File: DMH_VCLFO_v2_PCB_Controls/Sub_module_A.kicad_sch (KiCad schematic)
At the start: 93 parts, among them J34 Conn_02x03_Odd_Even, J35 Conn_02x03_Odd_Even, J36 Conn_02x03_Odd_Even, J37 Conn_02x03_Odd_Even, J38 Conn_02x03_Odd_Even, J39 Conn_02x03_Odd_Even, Q10 MMBFJ113, Q11 BC548, Q12 BC548, Q13 BC558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

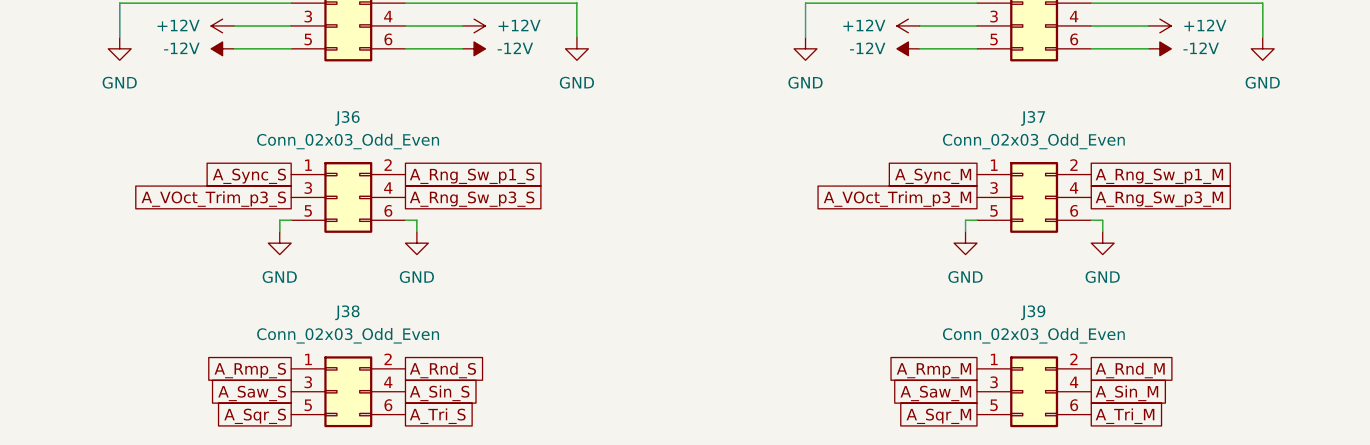
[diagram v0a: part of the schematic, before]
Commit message: Synced Controls PCB with Main
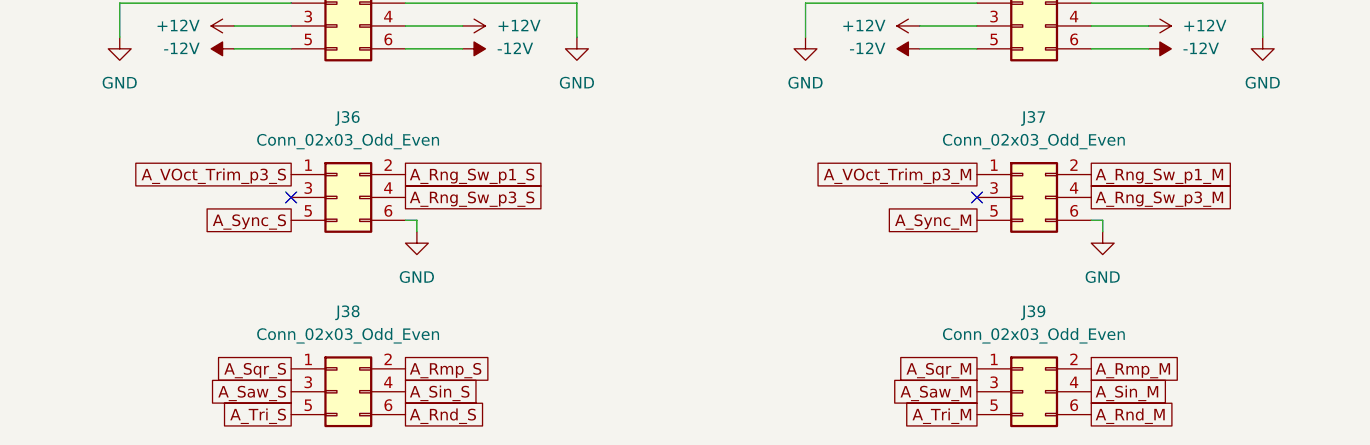
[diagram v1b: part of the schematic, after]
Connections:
- net A_Rmp_M: now also J39.2 (Pin_2); no longer J39.1 (Pin_1)
- net A_Rmp_S: now also J38.2 (Pin_2); no longer J38.1 (Pin_1)
- net A_Rnd_M: now also J39.6 (Pin_6); no longer J39.2 (Pin_2)
- net A_Rnd_S: now also J38.6 (Pin_6); no longer J38.2 (Pin_2)
- net A_Sqr_M: now also J39.1 (Pin_1); no longer J39.5 (Pin_5)
- net A_Sqr_S: now also J38.1 (Pin_1); no longer J38.5 (Pin_5)
- net A_Sync_M: now also J37.5 (Pin_5); no longer J37.1 (Pin_1)
- net A_Sync_S: now also J36.5 (Pin_5); no longer J36.1 (Pin_1)
- net A_Tri_M: now also J39.5 (Pin_5); no longer J39.6 (Pin_6)
- net A_Tri_S: now also J38.5 (Pin_5); no longer J38.6 (Pin_6)
- net A_VOct_Trim_p3_M: now also J37.1 (Pin_1); no longer J37.3 (Pin_3)
- net A_VOct_Trim_p3_S: now also J36.1 (Pin_1); no longer J36.3 (Pin_3)
- net GND: no longer J36.5 (Pin_5), J37.5 (Pin_5)
- no-connect marks 1 -> 3

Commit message: Generated Gerbers
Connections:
- net A_Rnd_S: now also U12.8, U12.9 (-); no longer U12.6 (-), U12.7
- net Comp_Ref: now also U12.2 (-); no longer U12.13 (-)
- net at D10.1 (K): now also U12.1; no longer U12.14
- net at Q9.1 (D), R71.1, R75.1: now also U12.14; no longer U12.1
- net at R71.2, R74.1: now also U12.13 (-); no longer U12.2 (-)
- net at R54.2, R61.1: now also U12.7; no longer U12.8
- net at C3.2, R73.1: now also U12.12 (+); no longer U12.3 (+)
- net at Q7.1 (C), R54.1, R56.2: now also U12.6 (-); no longer U12.9 (-)
- net at Q8.1 (C), R57.2, R66.1: now also U12.5 (+); no longer U12.10 (+)
- net at C6.1, R78.1: now also U12.3 (+); no longer U12.12 (+)
- net at C4.1, Q9.2 (S): now also U12.10 (+); no longer U12.5 (+)
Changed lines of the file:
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@@
 			)
 		)
+		(property "Function" ""
+			(at 243.84 254 0)
+			(effects
+				(font
+					(size 1.27 1.27)
+				)
+			)
+		)
 		(pin "10"
 		)
@@
 		(lib_id "Amplifier_Operational:TL074")
 		(at 69.85 95.25 0)
-		(unit 1)
+		(unit 4)
 		(exclude_from_sim no)
 		(in_bom yes)
@@
 				(path "/58f4306d-5387-4983-bb08-41a2313fd315/7ad2d702-dfb7-4d49-a82d-34430dd5948f"
 					(reference "U12")
-					(unit 1)
+					(unit 4)
 				)
 			)
@@
 		(lib_id "Amplifier_Operational:TL074")
 		(at 69.85 129.54 0)
-		(unit 4)
+		(unit 1)
 		(exclude_from_sim no)
 		(in_bom yes)
@@
 				(path "/58f4306d-5387-4983-bb08-41a2313fd315/7ad2d702-dfb7-4d49-a82d-34430dd5948f"
 					(reference "U12")
-					(unit 4)
+					(unit 1)
 				)
 			)
@@
 		(at 360.68 40.64 0)
 		(mirror x)
-		(unit 3)
+		(unit 2)
 		(exclude_from_sim no)
 		(in_bom yes)
@@
 				(path "/58f4306d-5387-4983-bb08-41a2313fd315/7ad2d702-dfb7-4d49-a82d-34430dd5948f"
 					(reference "U12")
-					(unit 3)
+					(unit 2)
 				)
 			)
@@
 		(lib_id "Amplifier_Operational:TL074")
 		(at 114.3 116.84 0)
-		(unit 2)
+		(unit 3)
 		(exclude_from_sim no)
 		(in_bom yes)
@@
 				(path "/58f4306d-5387-4983-bb08-41a2313fd315/7ad2d702-dfb7-4d49-a82d-34430dd5948f"
 					(reference "U12")
-					(unit 2)
+					(unit 3)
 				)
 			)
